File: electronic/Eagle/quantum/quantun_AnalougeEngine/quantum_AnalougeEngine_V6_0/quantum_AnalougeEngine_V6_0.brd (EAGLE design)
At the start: 210 x 70 mm, 279 parts, among them IC1 OP275, IC10 STM32F767ZIT6, IC11 PGA2320IDW, IC12 ESDA6V1BC6, IC13 USBLC6-4SC6, IC16 OP275, IC17 AD7606BSTZ-6, IC2 DAC084S085CIMM_NOPB, IC4 OP275, IC6 LAN8742A-CZ-TR, IC8 OP275, IC9 NE5532, J1 GWLEX-SMT-S988G_Y, K1 Relay, K2 Relay, K3 Relay, K4 Relay, K5 Relay, K6 Relay, K7 Relay, K8 Relay, T1 H1102NL, U1 78*_SMD, U12 ULN2003, U4 THAT1240, U6 THAT1240, U7 THAT1240, U8 THAT1240, Y1 NX3215SA-32.768K-STD-MUA-8, Y2 NX3225GD-8MHZ-STD-CRA-3, Y3 ABLS2-25.000MHZ-D4YF-T

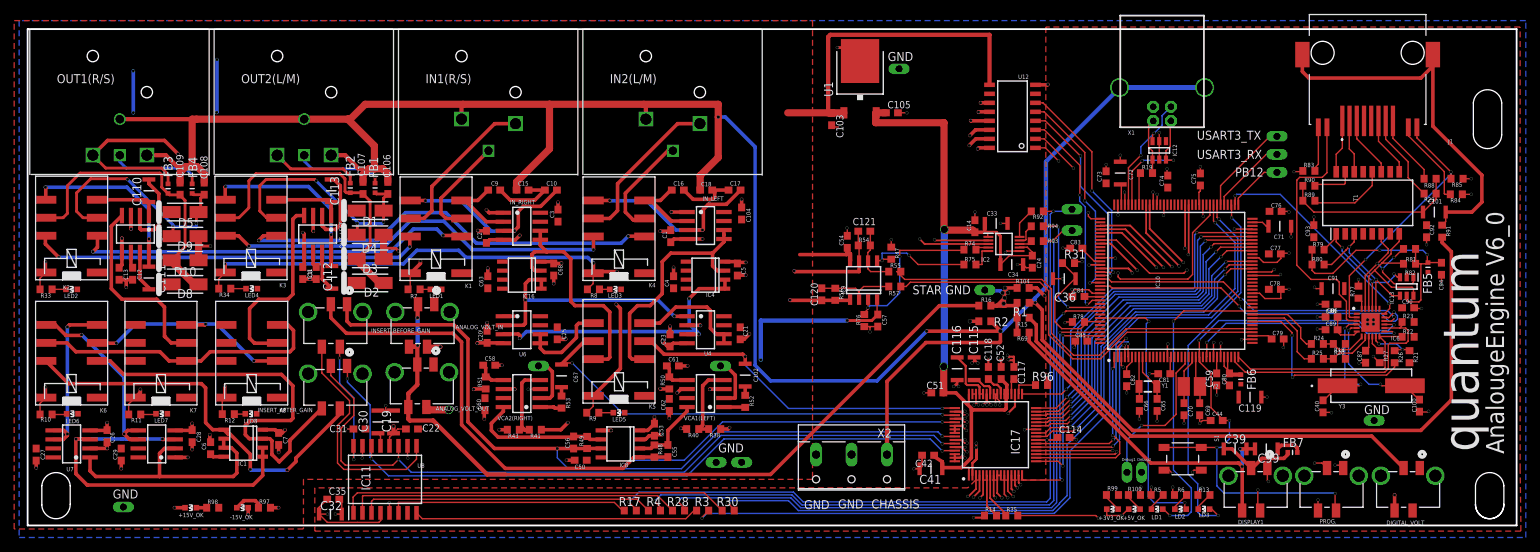
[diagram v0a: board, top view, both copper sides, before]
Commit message: OpenBLT TCP-IP -- UART Bridge
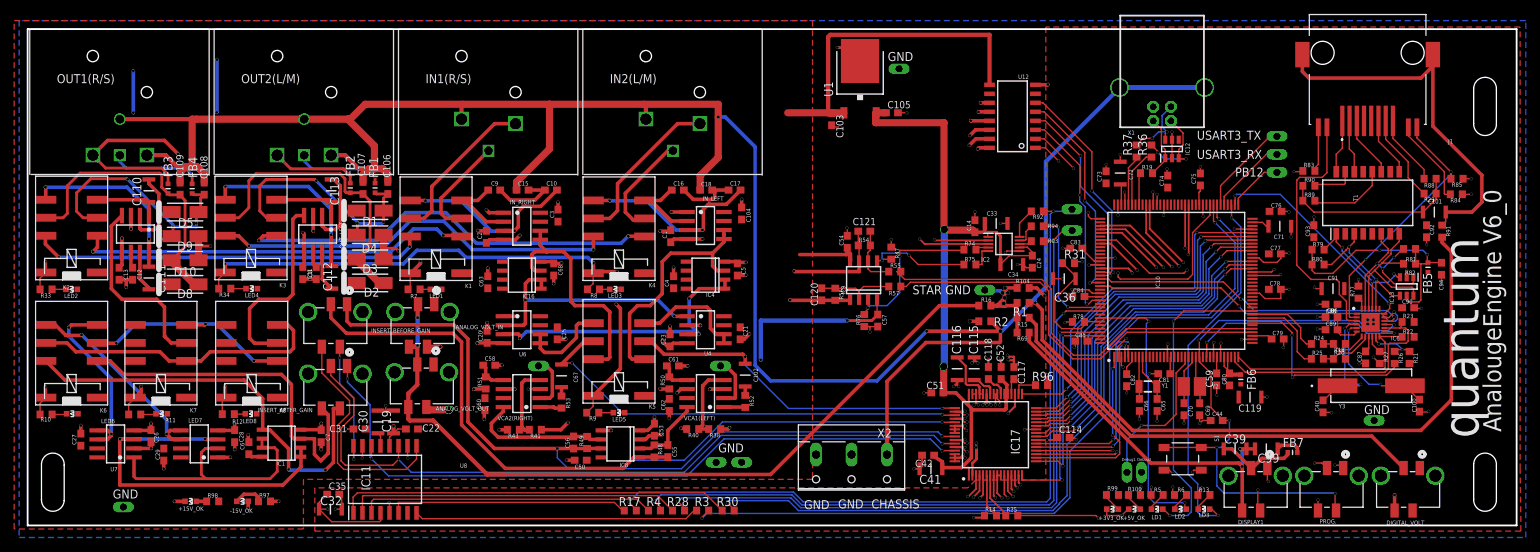
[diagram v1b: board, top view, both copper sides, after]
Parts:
- added R36, R37: 0 R, passive components:R0603
- moved C27 6.64 mm to (7.50, 12.1), turned to 90 degrees
- moved U7 6.20 mm to (12.4, 11.5)
- moved C26 6.20 mm to (17.4, 12.6)
- moved C7 6.01 mm to (41.4, 12.6)
- moved C28 6.00 mm to (29.2, 12.6)
- moved C29 6.00 mm to (19.2, 10.0)
- moved U8 6.00 mm to (24.2, 11.5)
- moved C6 5.40 mm to (31.2, 10.9)
- moved IC1 5.40 mm to (35.8, 11.6)
- moved IC12 1.81 mm to (161.4, 53.1)
- moved +15V_OK 0.90 mm to (23.0, 3.40)
- moved -15V_OK 0.90 mm to (30.3, 3.40)
- moved R97 0.90 mm to (33.4, 3.40)
- moved R98 0.90 mm to (26.1, 3.40)
- moved C35 0.70 mm to (43.1, 4.40)
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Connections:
- new net USB_N_AFTER: IC12.3, R36.2, X1.2
- new net USB_P_AFTER: IC12.6, R37.2, X1.3
- net USB_N: now also R36.1; no longer IC12.3, X1.2
- net USB_P: now also R37.1; no longer IC12.6, X1.3
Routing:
- net USB_N_AFTER: track 0.00 -> 13.1 mm, vias 0 -> 2
- net USB_P_AFTER: track 0.00 -> 10.6 mm, vias 0 -> 2
- net USB_P: track 17.5 -> 7.19 mm, vias 2 -> 0
- net USB_N: track 18.0 -> 8.29 mm, vias 2 -> 0
- net L/M_OUT(OUT_STAGE_LEFT): track 59.5 -> 51.1 mm
- net R/S_OUT(OUT_STAGE_RIGHT): track 56.3 -> 60.4 mm
- net S1: track 26.7 -> 29.2 mm
- net M1: track 24.1 -> 26.3 mm
- net N$43: track 35.1 -> 36.5 mm
- net N$45: track 52.4 -> 51.7 mm
- net USB_VBUS: track 8.08 -> 8.80 mm
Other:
- outline, holes or cut-outs redrawn

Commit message: AnaloougeEngine_V6_0 & PSU_V2_3
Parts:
- moved C82 0.20 mm to (155.0, 20.3)
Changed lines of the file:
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@@
 <setting verticaltext="up"/>
 </settings>
-<grid distance="1" unitdist="mm" unit="mm" style="lines" multiple="1" display="yes" altdistance="0.000123031496" altunitdist="mil" altunit="mil"/>
+<grid distance="0.1" unitdist="mm" unit="mm" style="lines" multiple="1" display="yes" altdistance="0.000123031496" altunitdist="mil" altunit="mil"/>
 <layers>
 <layer number="1" name="Top(V+/+3V3)" color="59" fill="1" visible="yes" active="yes"/>
@@
 <attribute name="VALUE" x="159.665" y="19.495" size="1.016" layer="27"/>
 </element>
-<element name="C82" library="passive components" library_urn="urn:adsk.eagle:library:16365137" package="C0603" package3d_urn="urn:adsk.eagle:package:576738/3" value="100 nF" x="155" y="20.5" smashed="yes" rot="R90">
-<attribute name="NAME" x="156.165" y="19.765" size="0.6096" layer="25" rot="R90"/>
-<attribute name="VALUE" x="156.905" y="19.865" size="1.016" layer="27" rot="R90"/>
+<element name="C82" library="passive components" library_urn="urn:adsk.eagle:library:16365137" package="C0603" package3d_urn="urn:adsk.eagle:package:576738/3" value="100 nF" x="155" y="20.3" smashed="yes" rot="R90">
+<attribute name="NAME" x="156.165" y="19.565" size="0.6096" layer="25" rot="R90"/>
+<attribute name="VALUE" x="156.905" y="19.665" size="1.016" layer="27" rot="R90"/>
 </element>
 <element name="C83" library="passive components" library_urn="urn:adsk.eagle:library:16365137" package="C0603" package3d_urn="urn:adsk.eagle:package:576738/3" value="100 nF" x="147.9" y="39.1" smashed="yes" rot="R180">
@@
 <wire x1="159.45" y1="21.4" x2="158.2" y2="21.4" width="0.2" layer="1"/>
 <via x="158.2" y="21.4" extent="1-16" drill="0.35"/>
-<wire x1="155" y1="19.65" x2="155" y2="18.7" width="0.2" layer="1"/>
-<via x="155" y="18.7" extent="1-16" drill="0.35"/>
+<wire x1="155" y1="19.45" x2="155" y2="18.5" width="0.2" layer="1"/>
+<via x="155" y="18.5" extent="1-16" drill="0.35"/>
 <wire x1="156.8" y1="16.15" x2="156.8" y2="15" width="0.2" layer="1"/>
 <via x="156.8" y="15" extent="1-16" drill="0.35"/>
@@
 <wire x1="165.25" y1="26.05" x2="165.25" y2="23.762" width="0.2" layer="1"/>
 <wire x1="192.7" y1="28.3" x2="191.9" y2="27.5" width="0.2" layer="16"/>
-<wire x1="191.9" y1="27.5" x2="189.1" y2="27.5" width="0.2" layer="16"/>
-<wire x1="189.1" y1="27.5" x2="187.7" y2="28.9" width="0.2" layer="16"/>
-<wire x1="187.7" y1="28.9" x2="168" y2="28.9" width="0.2" layer="16"/>
+<wire x1="191.9" y1="27.5" x2="188.6" y2="27.5" width="0.2" layer="16"/>
+<wire x1="188.6" y1="27.5" x2="187.2" y2="28.9" width="0.2" layer="16"/>
+<wire x1="187.2" y1="28.9" x2="168" y2="28.9" width="0.2" layer="16"/>
 <wire x1="168.55" y1="14.8" x2="168.7" y2="14.8" width="0.2" layer="1"/>
 <via x="169.5" y="14.8" extent="1-16" drill="0.35"/>
@@
 <wire x1="192.45" y1="27.35" x2="192.7" y2="27.1" width="0.2" layer="1"/>
 <via x="192.7" y="27.1" extent="1-16" drill="0.35"/>
-<wire x1="192.7" y1="27.1" x2="188.9" y2="27.1" width="0.2" layer="16"/>
-<wire x1="188.9" y1="27.1" x2="187.5" y2="28.5" width="0.2" layer="16"/>
-<wire x1="187.5" y1="28.5" x2="169" y2="28.5" width="0.2" layer="16"/>
+<wire x1="192.7" y1="27.1" x2="188.4" y2="27.1" width="0.2" layer="16"/>
+<wire x1="188.4" y1="27.1" x2="187" y2="28.5" width="0.2" layer="16"/>
+<wire x1="187" y1="28.5" x2="169" y2="28.5" width="0.2" layer="16"/>
 <wire x1="169" y1="28.5" x2="166.3" y2="25.8" width="0.2" layer="16"/>
 <via x="166.3" y="25.8" extent="1-16" drill="0.35"/>
@@
 <contactref element="C59" pad="2"/>
 <contactref element="C119" pad="2"/>
-<wire x1="155" y1="21.35" x2="155" y2="22.34165625" width="0.2" layer="1"/>
+<wire x1="155" y1="21.15" x2="155" y2="22.34165625" width="0.2" layer="1"/>
 <wire x1="155" y1="22.34165625" x2="155.75" y2="23.09165625" width="0.2" layer="1"/>
 <wire x1="155.75" y1="23.09165625" x2="155.75" y2="23.762" width="0.2" layer="1"/>
@@
 <contactref element="C89" pad="2"/>
 <contactref element="C88" pad="2"/>
-<wire x1="187.45" y1="27.35" x2="187.45" y2="27.24895625" width="0.2" layer="1"/>
-<wire x1="187.45" y1="27.24895625" x2="187.07604375" y2="26.875" width="0.2" layer="1"/>
+<wire x1="187.45" y1="27.35" x2="187.500521875" y2="27.299478125" width="0.2" layer="1"/>
+<wire x1="187.500521875" y1="27.299478125" x2="187.07604375" y2="26.875" width="0.2" layer="1"/>
 <wire x1="187.07604375" y1="26.875" x2="185.175" y2="26.875" width="0.2" layer="1"/>
 <wire x1="185.175" y1="26.875" x2="184.75" y2="27.3" width="0.2" layer="1"/>
